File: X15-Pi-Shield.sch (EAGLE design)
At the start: 76 parts, among them J1 T2I, J2 T2I, J3 DF13-4P-1.25DSA, J4 T2I, J5 DF13-4P-1.25DSA, J6 DF13-4P-1.25DSA, Q1 220mA/50V/3.5Ω, Q2 2.5A/30V/105mΩ, Q3 220mA/50V/3.5Ω, Q4 220mA/50V/3.5Ω, Q5 220mA/50V/3.5Ω, U1 ULN2003AD, U2 MAX1136EUA-T, Y2 ECS-80-S-4X

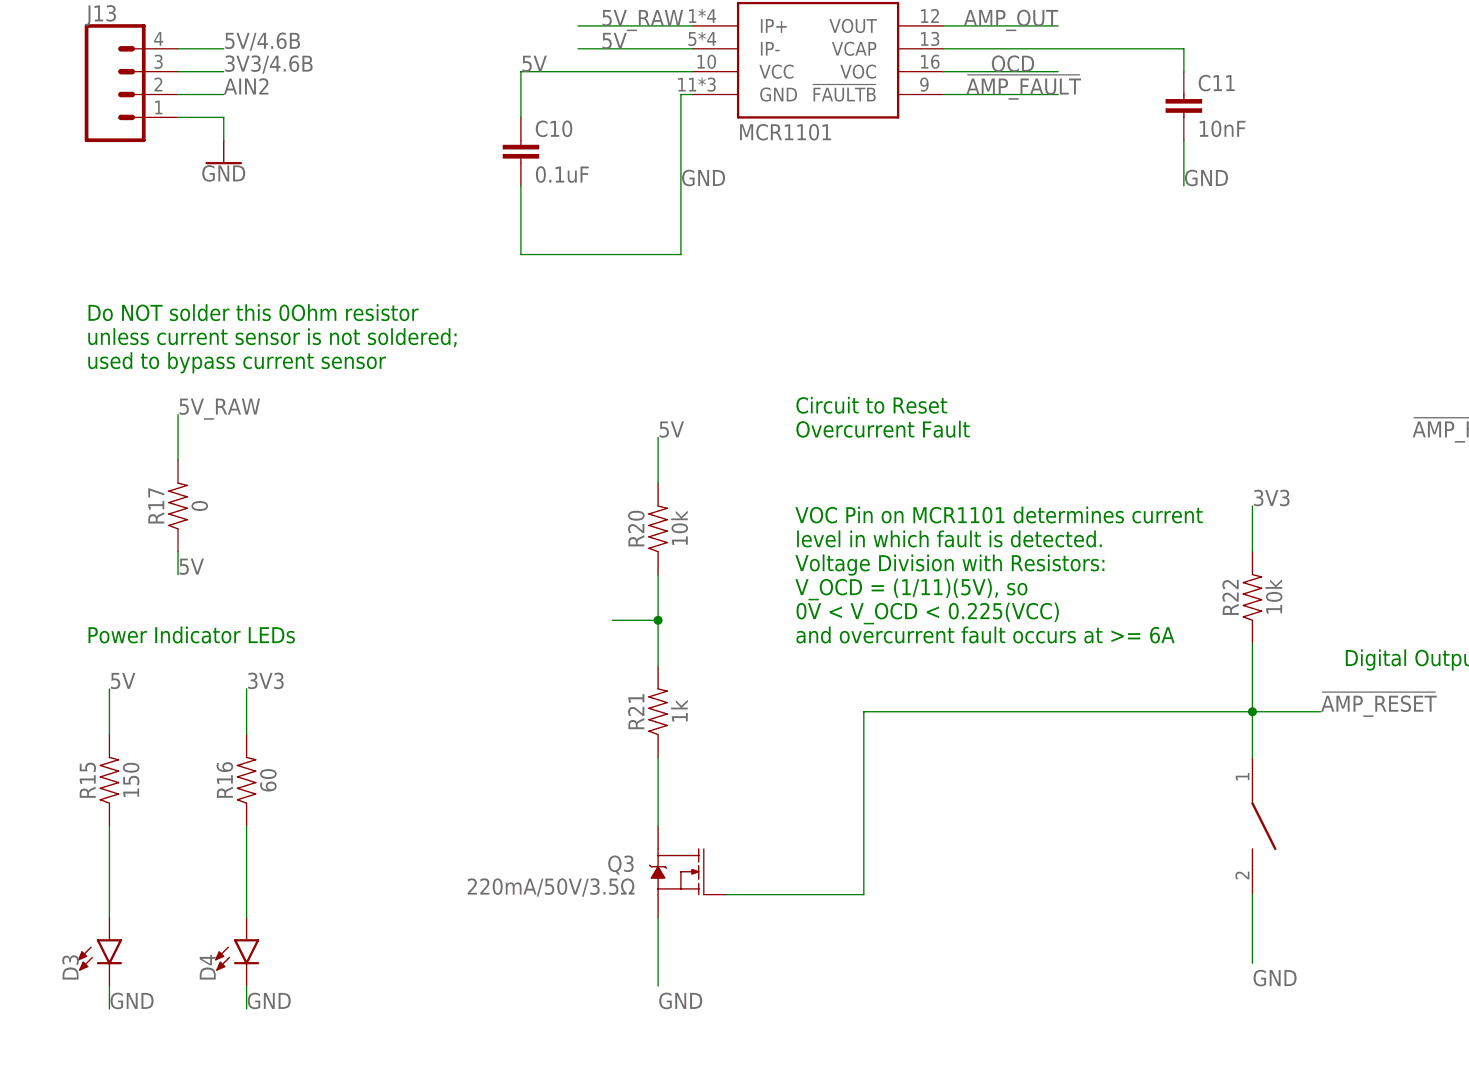
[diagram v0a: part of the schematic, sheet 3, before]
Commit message: fixed ground and parts library
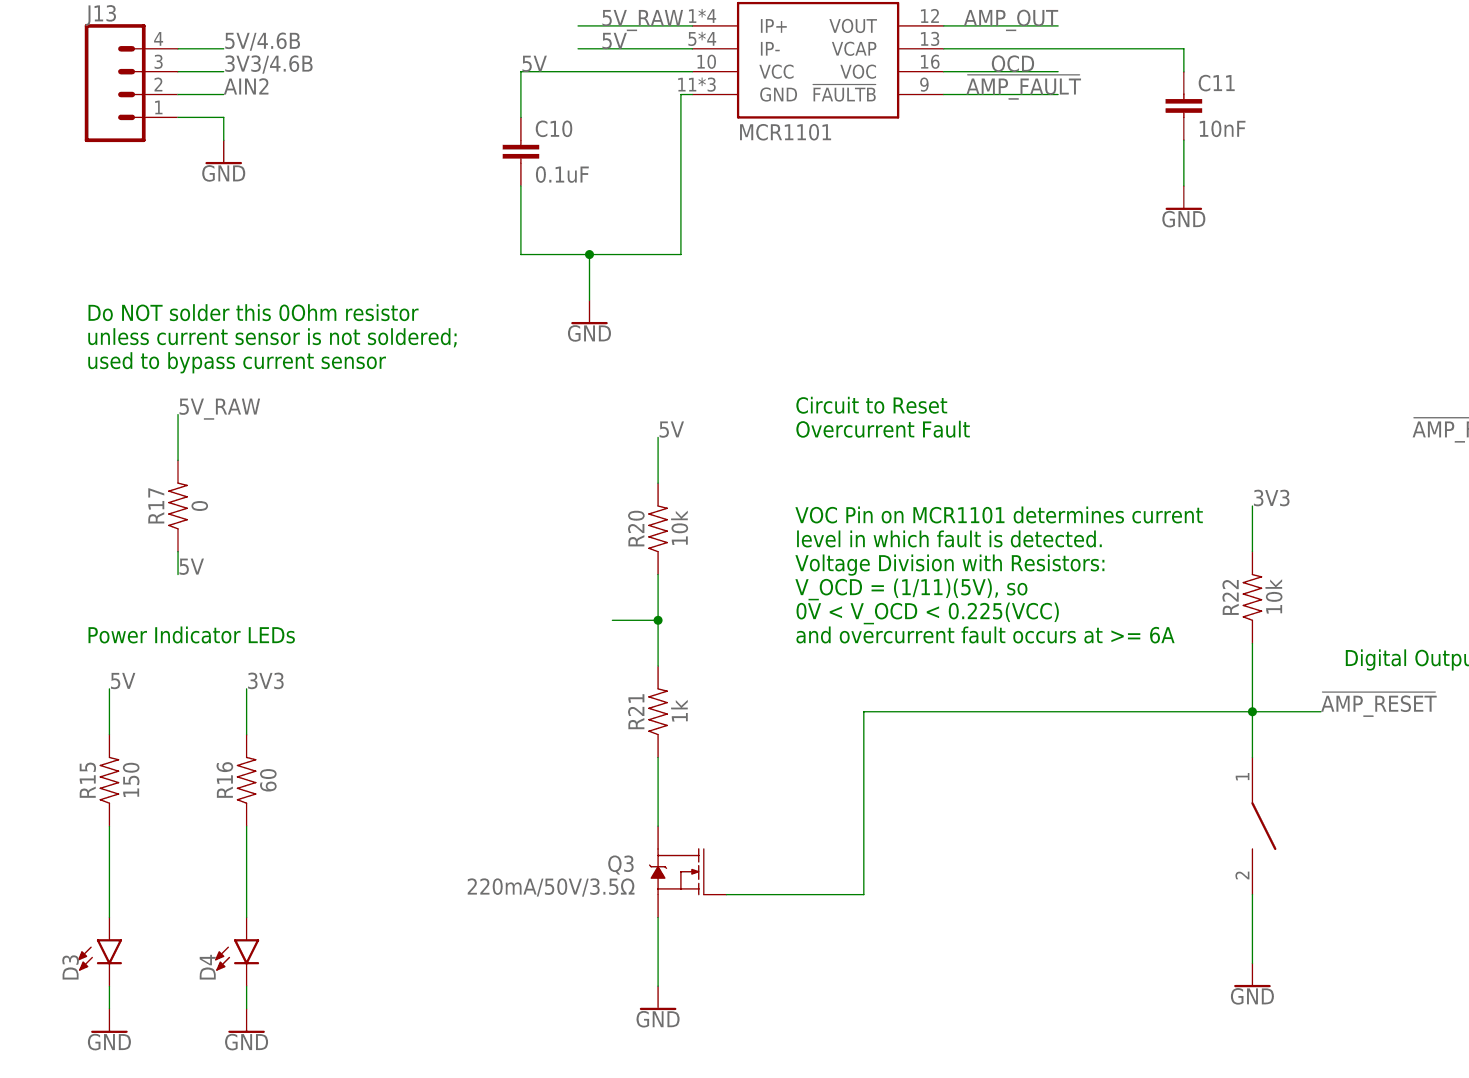
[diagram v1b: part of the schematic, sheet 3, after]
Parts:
- removed C8: 150uF, CAP, Tantalum 150 uF - Kemet 2917 T491:C-TANTALUM(10UF_150UF)
- added C14: 150uF, X15-Pi-Shield-Parts:C-TANTALUM(10UF_150UF)
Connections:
- net GND: now also C14.-; no longer C8.-
- net PI_POWER: now also C14.+; no longer C8.+
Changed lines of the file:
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@@
 <part name="R13" library="SparkFun-Resistors" library_urn="urn:adsk.eagle:library:532" deviceset="RESISTOR" device="0603" package3d_urn="urn:adsk.eagle:package:39650/1" value="0"/>
 <part name="R14" library="SparkFun-Resistors" library_urn="urn:adsk.eagle:library:532" deviceset="RESISTOR" device="0603" package3d_urn="urn:adsk.eagle:package:39650/1" value="0"/>
-<part name="C8" library="CAP, Tantalum 150 uF - Kemet 2917 T491" deviceset="C-TANTALUM(10UF_150UF)" device="" package3d_urn="urn:adsk.eagle:package:25131320/3" value="150uF"/>
 <part name="GND21" library="SparkFun-PowerSymbols" library_urn="urn:adsk.eagle:library:530" deviceset="GND" device=""/>
 <part name="J3" library="X15-Pi-Shield-Parts" deviceset="DF13-4P-1.25" device="DSA"/>
@@
 <part name="C13" library="SparkFun-Capacitors" library_urn="urn:adsk.eagle:library:510" deviceset="0.1UF" device="-0603-25V-(+80/-20%)" package3d_urn="urn:adsk.eagle:package:37414/1" value="0.1uF"/>
 <part name="GND36" library="SparkFun-PowerSymbols" library_urn="urn:adsk.eagle:library:530" deviceset="GND" device=""/>
+<part name="GND37" library="SparkFun-PowerSymbols" library_urn="urn:adsk.eagle:library:530" deviceset="GND" device=""/>
+<part name="GND38" library="SparkFun-PowerSymbols" library_urn="urn:adsk.eagle:library:530" deviceset="GND" device=""/>
+<part name="GND39" library="SparkFun-PowerSymbols" library_urn="urn:adsk.eagle:library:530" deviceset="GND" device=""/>
+<part name="GND40" library="SparkFun-PowerSymbols" library_urn="urn:adsk.eagle:library:530" deviceset="GND" device=""/>
+<part name="GND41" library="SparkFun-PowerSymbols" library_urn="urn:adsk.eagle:library:530" deviceset="GND" device=""/>
+<part name="GND42" library="SparkFun-PowerSymbols" library_urn="urn:adsk.eagle:library:530" deviceset="GND" device=""/>
+<part name="GND43" library="SparkFun-PowerSymbols" library_urn="urn:adsk.eagle:library:530" deviceset="GND" device=""/>
+<part name="GND44" library="SparkFun-PowerSymbols" library_urn="urn:adsk.eagle:library:530" deviceset="GND" device=""/>
+<part name="C14" library="X15-Pi-Shield-Parts" deviceset="C-TANTALUM(10UF_150UF)" device="" package3d_urn="urn:adsk.eagle:package:25131320/3" value="150uF"/>
 </parts>
 <sheets>
@@
 <attribute name="VALUE" x="231.14" y="84.836" size="1.778" layer="96" font="vector" align="top-center"/>
 </instance>
-<instance part="C8" gate="G$1" x="241.3" y="81.28" smashed="yes">
-<attribute name="NAME" x="242.316" y="81.915" size="1.778" layer="95"/>
-<attribute name="VALUE" x="242.316" y="77.089" size="1.778" layer="96"/>
-</instance>
 <instance part="GND21" gate="1" x="241.3" y="71.12" smashed="yes">
 <attribute name="VALUE" x="241.3" y="70.866" size="1.778" layer="96" align="top-center"/>
@@
 <instance part="GND29" gate="1" x="246.38" y="43.18" smashed="yes">
 <attribute name="VALUE" x="246.38" y="42.926" size="1.778" layer="96" align="top-center"/>
+</instance>
+<instance part="C14" gate="G$1" x="241.3" y="81.28" smashed="yes">
+<attribute name="NAME" x="242.316" y="81.915" size="1.778" layer="95"/>
+<attribute name="VALUE" x="242.316" y="77.089" size="1.778" layer="96"/>
 </instance>
 </instances>
@@
 <pinref part="R14" gate="G$1" pin="2"/>
 <wire x1="236.22" y1="86.36" x2="241.3" y2="86.36" width="0.1524" layer="91"/>
-<pinref part="C8" gate="G$1" pin="+"/>
 <wire x1="241.3" y1="86.36" x2="241.3" y2="83.82" width="0.1524" layer="91"/>
 <pinref part="R13" gate="G$1" pin="2"/>
@@
 <junction x="241.3" y="88.9"/>
 <label x="243.84" y="88.9" size="1.778" layer="95"/>
+<pinref part="C14" gate="G$1" pin="+"/>
 </segment>
 </net>
@@
 </segment>
 <segment>
-<pinref part="C8" gate="G$1" pin="-"/>
 <wire x1="241.3" y1="76.2" x2="241.3" y2="73.66" width="0.1524" layer="91"/>
 <pinref part="GND21" gate="1" pin="GND"/>
+<pinref part="C14" gate="G$1" pin="-"/>
 </segment>
 <segment>
@@
 <attribute name="VALUE" x="157.48" y="124.206" size="1.778" layer="96" align="top-center"/>
 </instance>
+<instance part="GND39" gate="1" x="78.74" y="7.62" smashed="yes">
+<attribute name="VALUE" x="78.74" y="7.366" size="1.778" layer="96" align="top-center"/>
+</instance>
+<instance part="GND40" gate="1" x="144.78" y="10.16" smashed="yes">
+<attribute name="VALUE" x="144.78" y="9.906" size="1.778" layer="96" align="top-center"/>
+</instance>
+<instance part="GND41" gate="1" x="71.12" y="83.82" smashed="yes">
+<attribute name="VALUE" x="71.12" y="83.566" size="1.778" layer="96" align="top-center"/>
+</instance>
+<instance part="GND42" gate="1" x="137.16" y="96.52" smashed="yes">
+<attribute name="VALUE" x="137.16" y="96.266" size="1.778" layer="96" align="top-center"/>
+</instance>
+<instance part="GND43" gate="1" x="17.78" y="5.08" smashed="yes">
+<attribute name="VALUE" x="17.78" y="4.826" size="1.778" layer="96" align="top-center"/>
+</instance>
+<instance part="GND44" gate="1" x="33.02" y="5.08" smashed="yes">
+<attribute name="VALUE" x="33.02" y="4.826" size="1.778" layer="96" align="top-center"/>
+</instance>
 </instances>
 <busses>
@@
 <pinref part="D4" gate="G$1" pin="C"/>
 <wire x1="33.02" y1="10.16" x2="33.02" y2="7.62" width="0.1524" layer="91"/>
-<label x="33.02" y="7.62" size="1.778" layer="95"/>
+<pinref part="GND44" gate="1" pin="GND"/>
 </segment>
 <segment>
 <pinref part="D3" gate="G$1" pin="C"/>
 <wire x1="17.78" y1="10.16" x2="17.78" y2="7.62" width="0.1524" layer="91"/>
-<label x="17.78" y="7.62" size="1.778" layer="95"/>
+<pinref part="GND43" gate="1" pin="GND"/>
 </segment>
 <segment>
@@
 </segment>
 <segment>
-<pinref part="Q3" gate="NMOS" pin="S"/>
-<wire x1="78.74" y1="17.78" x2="78.74" y2="10.16" width="0.1524" layer="91"/>
-<label x="78.74" y="7.62" size="1.778" layer="95"/>
-</segment>
-<segment>
-<pinref part="U$7" gate="G$1" pin="P$2"/>
-<wire x1="144.78" y1="20.32" x2="144.78" y2="12.7" width="0.1524" layer="91"/>
-<label x="144.78" y="10.16" size="1.778" layer="95"/>
-</segment>
-<segment>
 <pinref part="C10" gate="G$1" pin="2"/>
 <wire x1="63.5" y1="99.06" x2="63.5" y2="91.44" width="0.1524" layer="91"/>
-<wire x1="63.5" y1="91.44" x2="81.28" y2="91.44" width="0.1524" layer="91"/>
+<wire x1="63.5" y1="91.44" x2="71.12" y2="91.44" width="0.1524" layer="91"/>
+<wire x1="71.12" y1="91.44" x2="81.28" y2="91.44" width="0.1524" layer="91"/>
 <wire x1="81.28" y1="91.44" x2="81.28" y2="109.22" width="0.1524" layer="91"/>
 <pinref part="U$8" gate="G$1" pin="GND"/>
 <wire x1="81.28" y1="109.22" x2="82.55" y2="109.22" width="0.1524" layer="91"/>
-<label x="81.28" y="99.06" size="1.778" layer="95"/>
+<pinref part="GND41" gate="1" pin="GND"/>
+<wire x1="71.12" y1="91.44" x2="71.12" y2="86.36" width="0.1524" layer="91"/>
+<junction x="71.12" y="91.44"/>
 </segment>
 <segment>
 <pinref part="C11" gate="G$1" pin="2"/>
 <wire x1="137.16" y1="104.14" x2="137.16" y2="99.06" width="0.1524" layer="91"/>
-<label x="137.16" y="99.06" size="1.778" layer="95"/>
+<pinref part="GND42" gate="1" pin="GND"/>
 </segment>
 <segment>
@@
 <wire x1="157.48" y1="129.54" x2="157.48" y2="127" width="0.1524" layer="91"/>
 <pinref part="GND36" gate="1" pin="GND"/>
+</segment>
+<segment>
+<pinref part="Q3" gate="NMOS" pin="S"/>
+<pinref part="GND39" gate="1" pin="GND"/>
+<wire x1="78.74" y1="17.78" x2="78.74" y2="10.16" width="0.1524" layer="91"/>
+</segment>
+<segment>
+<pinref part="U$7" gate="G$1" pin="P$2"/>
+<pinref part="GND40" gate="1" pin="GND"/>
+<wire x1="144.78" y1="20.32" x2="144.78" y2="12.7" width="0.1524" layer="91"/>
 </segment>
 </net>
@@
 </instance>
 <instance part="U1" gate="G$1" x="76.2" y="134.62" smashed="yes"/>
+<instance part="GND37" gate="1" x="76.2" y="104.14" smashed="yes">
+<attribute name="VALUE" x="76.2" y="103.886" size="1.778" layer="96" align="top-center"/>
+</instance>
+<instance part="GND38" gate="1" x="88.9" y="60.96" smashed="yes">
+<attribute name="VALUE" x="88.9" y="60.706" size="1.778" layer="96" align="top-center"/>
+</instance>
 </instances>
 <busses>
@@
 </segment>
 <segment>
+<pinref part="U1" gate="G$1" pin="GND"/>
+<wire x1="76.2" y1="111.76" x2="76.2" y2="106.68" width="0.1524" layer="91"/>
+<pinref part="GND37" gate="1" pin="GND"/>
+</segment>
+<segment>
 <pinref part="C9" gate="G$1" pin="-"/>
 <wire x1="88.9" y1="68.58" x2="88.9" y2="63.5" width="0.1524" layer="91"/>
-<label x="83.82" y="63.5" size="1.778" layer="95"/>
-</segment>
-<segment>
-<pinref part="U1" gate="G$1" pin="GND"/>
-<wire x1="76.2" y1="111.76" x2="76.2" y2="99.06" width="0.1524" layer="91"/>
-<label x="76.2" y="101.6" size="1.778" layer="95" rot="R90"/>
-</segment>
-</net>
+<pinref part="GND38" gate="1" pin="GND"/>
+</segment>
+</net>

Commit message: help me mr. bryce sir
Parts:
- removed J8: (no value), SparkFun-Connectors:CONN_03
- added R27, R28, R29, R30: (no value), SparkFun-Resistors:RESISTOR0603
- added U$9: 8X_CONN, X15-Pi-Shield-Parts:8X_CONN
- U$1: value TCAN337D -> MAX3058; device X15-Pi-Shield-Parts:TCAN337D -> X15-Pi-Shield-Parts:MAX3058
- U$6: value 7X_CONN -> HI-3110; device X15-Pi-Shield-Parts:7X_CONN -> X15-Pi-Shield-Parts:HI-3110
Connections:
- removed net 3V3/1.5D: J3.1, J5.1, J6.1
- removed net 3V3/2.5C: C5.1, C6.1, D1.C, JP1.2, R4.2, R6.1, U$1.VCC, U$2.VDD
- removed net 3V3/3.2B: C7.1, J11.4, R10.2, U$3.VIN, U$5.VIN
- removed net 3V3/4.6B: J13.3, J14.2, J15.2
- removed net 5V/1.7D: J8.2, R13.1, R14.1
- removed net 5V/2.7C: C13.1, U2.AIN3/REF
- removed net 5V/2.7D: J2.1
- removed net 5V/4.6B: C12.1, J13.4, U2.VDD
- removed net AMP_RESET/3.4E: U$4.GPIO4
- removed net CAN_H/2.8D: J1.2, J4.2, R8.2, U$1.CANH
- removed net CAN_H/4.7B: J10.2
- removed net CAN_L/2.8D: J1.3, J4.3, R9.1, U$1.CANL
- removed net CAN_L/4.6B: J10.1
- removed net CAN_RESET/1.4C: U$4.GPIO22
- removed net CAN_RESET/2.2D: R5.1
- removed net CLK/1.2B: J12.2, U$4.GPIO11
- removed net CLK/2.2C: U$2.SCK
- removed net CS/1.2A: J12.5, U$4.GPIO8
- removed net CS/2.1C: U$2.CS
- removed net DI1/1.7D: U$4.GPIO16
- removed net DI1/2.1C: J2.2
- removed net DI2/1.7D: U$4.GPIO20
- removed net DI2/2.1B: J2.3
- removed net GPIO1/4.2B: U$4.GPIO18
- removed net GPIO2/4.2B: U$4.GPIO23
- removed net GPIO3/4.2B: U$4.GPIO24
- removed net GPIO4/4.2B: U$4.GPIO25
- removed net GPIO5/4.2B: U$4.GPIO12
- removed net GPIO6/4.2B: U$4.GPIO21
- removed net INT/1.2B: U$4.GPIO26
- removed net INT/2.2B: U$2.INT
- removed net MISO/1.2B: J12.4, U$4.GPIO9
- removed net MISO/2.2D: U$2.SO
- removed net MOSI/1.2B: J12.3, U$4.GPIO10
- removed net MOSI/2.2D: U$2.SI
- removed net RX0_INT/1.2B: U$4.GPIO19
- removed net RX0_INT/2.2C: U$2.RX0BF
- removed net RX1_INT/1.2B: U$4.GPIO5
- removed net RX1_INT/2.2C: U$2.RX1BF
- removed net SCL/3.6C: J11.2, J3.2, J5.2, J6.2, J7.2, U$3.SCL, U$4.GPIO3
- removed net SDA/3.7C: J11.3, J3.3, J5.3, J6.3, J7.3, U$3.SDA, U$4.GPIO2
- new net CAN_RESET: R27.2, R5.1, U$4.GPIO22, U$6.MR
- new net CLK: J12.2, R30.2, U$2.SCK, U$4.GPIO11, U$6.SCK
- new net CS: J12.5, R28.2, U$2.CS, U$4.GPIO8, U$6.CS
- new net DI1: J2.2, U$4.GPIO16
- new net DI2: J2.3, U$4.GPIO20
- new net INT: U$2.INT, U$4.GPIO26, U$6.INT
- new net MISO: J12.4, U$2.SO, U$4.GPIO9, U$6.SO
- new net MOSI: J12.3, R29.2, U$2.SI, U$4.GPIO10, U$6.SI
- new net N$17: U$6.GP1
- new net N$18: U$6.GP2
- new net N$19: U$6.TXEN
- new net N$20: U$6.SPLIT
- new net ROBOT_ARM: U$9.4
- new net RX0_INT: U$2.RX0BF, U$4.GPIO19
- new net RX1_INT: U$2.RX1BF, U$4.GPIO5
- net !AMP_RESET: now also U$4.GPIO4
- net 12V: now also U$9.13, U$9.15; no longer U$6.13, U$6.15
- net 3V3: now also C5.1, C6.1, C7.1, D1.C, J11.4, J13.3, J14.2, J15.2, J3.1, J5.1, J6.1, JP1.2, R10.2, R28.1, R4.2, R6.1, U$1.VCC, U$2.VDD, U$3.VIN, U$5.VIN, U$6.VLOGIC, U$9.23; no longer U$6.23
- net 5V: now also C12.1, C13.1, J13.4, J2.1, R13.1, R14.1, U$6.VDD, U$9.19, U2.AIN3/REF, U2.VDD; no longer U$6.19
- net CAN_H: now also J1.2, J10.2, J4.2, R8.2, U$1.CANH, U$6.CANH, U$9.1; no longer U$6.1
- net CAN_L: now also J1.3, J10.1, J4.3, R9.1, U$1.CANL, U$6.CANL, U$9.2; no longer U$6.2
- net CAN_SILENT: now also U$1.RS; no longer U$1.S
- net FAULT: now also U$1.SHDN; no longer U$1.FAULT
- net GND: now also R27.1, R29.1, R30.1, U$6.GND, U$9.17, U$9.21; no longer J8.1, U$6.17, U$6.21
- net GPIO1: now also U$4.GPIO18
- net GPIO2: now also U$4.GPIO23
- net GPIO3: now also U$4.GPIO24
- net GPIO4: now also U$4.GPIO25
- net GPIO5: now also U$4.GPIO12
- net GPIO6: now also U$4.GPIO21
- net OSC1: now also U$6.OSCIN
- net OSC2: now also U$6.OSCOUT
- net PWM: no longer J8.3
- net SCL: now also J11.2, J3.2, J5.2, J6.2, J7.2, U$3.SCL, U$4.GPIO3
- net SDA: now also J11.3, J3.3, J5.3, J6.3, J7.3, U$3.SDA, U$4.GPIO2
- net SOL1_1: now also U$9.14; no longer U$6.14
- net SOL2_1: now also U$9.16; no longer U$6.16
- net SOL3_1: now also U$9.18; no longer U$6.18
- net SOL4_1: now also U$9.20; no longer U$6.20
- net SOL5_1: now also U$9.22; no longer U$6.22
- net SOL6_1: now also U$9.24; no longer U$6.24
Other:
- note added: "ONE OF THESE PINS GOES TO ROBOT ARM"
- note added: "PIN 15 is a new addition for PWM signal to the robot arm"
- note removed: "Servo Connector"
- moved on the sheet: C4, C5, C6, J1, J2, J4, JP1, R8, R9, U$1, U$2

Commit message: hi
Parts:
- removed C3: 22nF, SparkFun-Capacitors:22NF/22,000PF-0603-50V-10%
- removed C5, C6: 0.1uF, SparkFun-Capacitors:0.1UF-0603-25V-(+80/-20%)
- removed D1: 250mA/100V, SparkFun-DiscreteSemi:DIODE-BAS16J
- removed JP1: JUMPER-SMT_2_NO_SILK, SparkFun-Jumpers:JUMPER-SMT_2_NO_SILK
- removed R3, R5: 1k, SparkFun-Resistors:RESISTOR0603
- removed R4: 10k, SparkFun-Resistors:RESISTOR0603
- removed U$1: MAX3058, X15-Pi-Shield-Parts:MAX3058
- removed U$2: MCP2515, X15-Pi-Shield-Parts:MCP2515
- R27, R28, R29, R30: value (none) -> 50k
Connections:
- removed net CAN_SILENT: JP1.1, U$1.RS
- removed net N$17: U$6.GP1
- removed net N$18: U$6.GP2
- removed net N$19: U$6.TXEN
- removed net N$20: U$6.SPLIT
- removed net N$4: C3.1, D1.A, R3.2, R4.1, R5.2
- removed net RESET: R3.1, U$2.RESET
- removed net RXCAN: U$1.RXD, U$2.RXCAN
- removed net TXCAN: U$1.TXD, U$2.TXCAN
- net 3V3: now also U$6.TXEN; no longer C5.1, C6.1, D1.C, JP1.2, R4.2, U$1.VCC, U$2.VDD
- net CAN_H: no longer U$1.CANH
- net CAN_L: no longer U$1.CANL
- net CAN_RESET: no longer R5.1
- net CLK: no longer U$2.SCK
- net CS: no longer U$2.CS
- net FAULT: no longer U$1.SHDN
- net GND: no longer C3.2, C5.2, C6.2, U$1.GND, U$2.VSS
- net INT: no longer U$2.INT
- net MISO: no longer U$2.SO
- net MOSI: no longer U$2.SI
- net OSC1: no longer U$2.OSC1
- net OSC2: no longer U$2.OSC2
- net RX0_INT: now also U$6.GP1; no longer U$2.RX0BF
- net RX1_INT: now also U$6.GP2; no longer U$2.RX1BF
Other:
- note added: "GENERAL PURPOSE PINS CONNECTED TO RX0_INT AND RX1_INT, NOT SURE IF THIS IS RIGHT"
- note removed: "CAN Controller"
- note removed: "CAN Transceiver"
- note removed: "Pull S pin high for silent mode Silent mode is unwanted Do not populate JP1"
- moved on the sheet: R27, R28, R29, R30

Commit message: I'm slowly losing my mind
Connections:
- net ROBOT_ARM: now also U$4.GPIO6
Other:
- note added: "IS THIS NEEDED ANYMORE??? FAULT NOT CONNECTED TO ANYTHING"
- note removed: "Potential pH Sensor Connector"
- note removed: "Pressure Sensor Connector"
- note removed: "Temperature Sensor Connector"
- moved on the sheet: J3, J5, J6
